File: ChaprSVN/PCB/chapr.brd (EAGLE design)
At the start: 70.9 x 54.1 mm, 20 parts, among them M2 RN42 Module

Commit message: Intermediate version with new power-on circuit.  NOT COMPLETE.
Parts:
- added D1, D2: 1N4148, diode:DO35-7
- added PB2: BUTTON, ChapR-Custom:2-PIN-PUSHBUTTON
- added R12, R13, R15: 12k, resistor:0207/10
- added R14: 22k, resistor:0207/10
- added T1, T2: (no value), transistor:TO92
- moved JP1 18.7 mm to (66.4, 54.0), turned to 0 degrees
- moved R5 16.1 mm to (10.3, 42.1)
- moved R4 16.1 mm to (10.2, 45.7)
- moved R7 15.2 mm to (38.1, 42.2)
- moved R8 15.2 mm to (38.2, 45.6)
- moved R1 15.0 mm to (24.2, 45.6)
- moved R2 14.9 mm to (24.2, 42.0)
- moved R11 6.91 mm to (24.7, 23.4)
- moved R9 6.71 mm to (10.5, 23.5)
- moved R6 6.02 mm to (24.7, 26.5)
- moved R3 5.83 mm to (10.4, 26.5)
- moved ARDUINO 4.00 mm to (17.8, 25.8)
- moved VDIP 2.00 mm to (36.2, 44.2)
- moved U$2 1.00 mm to (61.0, 7.23)
- renumbered LED2 to PWR-LED
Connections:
- net 3.3V renamed +3V3
- new net +5V: ARDUINO.VCC, PB1.P$1, R12.1, VDIP.2, VDIP.3, VDIP.9
- new net N$23: ARDUINO.RAWV, T1.3
- new net N$25: D2.A, R15.2, T2.3
- new net N$26: R13.1, T2.2
- new net N$27: D1.C, D2.C, PB2.P$2
- new net N$29: ARDUINO.A5, D1.A, R12.2
- new net N$30: ARDUINO.A4, R13.2
- net +9V: now also R14.2, T1.1; no longer ARDUINO.RAWV
- net GND: now also PB2.P$1, T2.1
- net N$1: now also R14.1, R15.1, T1.2; no longer ARDUINO.VCC, PB1.P$1, VDIP.2, VDIP.3, VDIP.9
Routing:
- net +5V: track 0.00 -> 168.9 mm, vias 0 -> 4
- net N$25: track 0.00 -> 90.4 mm, vias 0 -> 3
- net N$23: track 0.00 -> 89.3 mm, vias 0 -> 1
- net N$29: track 0.00 -> 79.2 mm, vias 0 -> 1
- net N$1: track 95.2 -> 24.4 mm, vias 1 -> 0
- net +9V: track 84.6 -> 15.2 mm
- net N$22: track 76.9 -> 132.4 mm, vias 0 -> 3
- net GND: track 176.5 -> 222.9 mm
- net N$30: track 0.00 -> 40.7 mm, vias 0 -> 1
- net N$27: track 0.00 -> 33.2 mm
- net N$12: track 65.0 -> 93.6 mm, vias 0 -> 2
- net N$13: track 63.4 -> 36.5 mm, vias 1 -> 2
- net N$18: track 50.5 -> 26.9 mm, vias 1 -> 0
- net N$7: track 40.0 -> 63.5 mm
- net N$14: track 61.8 -> 81.9 mm, vias 0 -> 7
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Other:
- board size 70.9 x 54.1 mm -> 70.9 x 56.2 mm

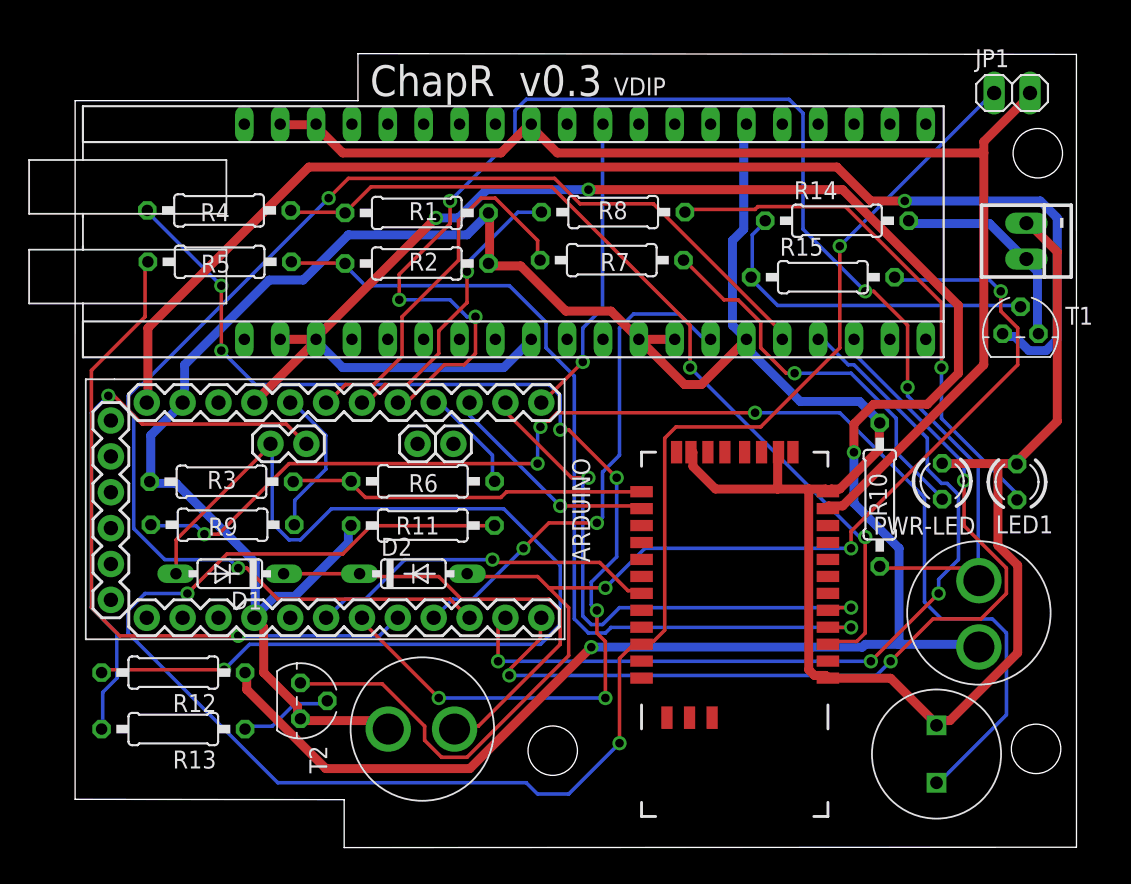
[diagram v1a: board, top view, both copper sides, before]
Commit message: 
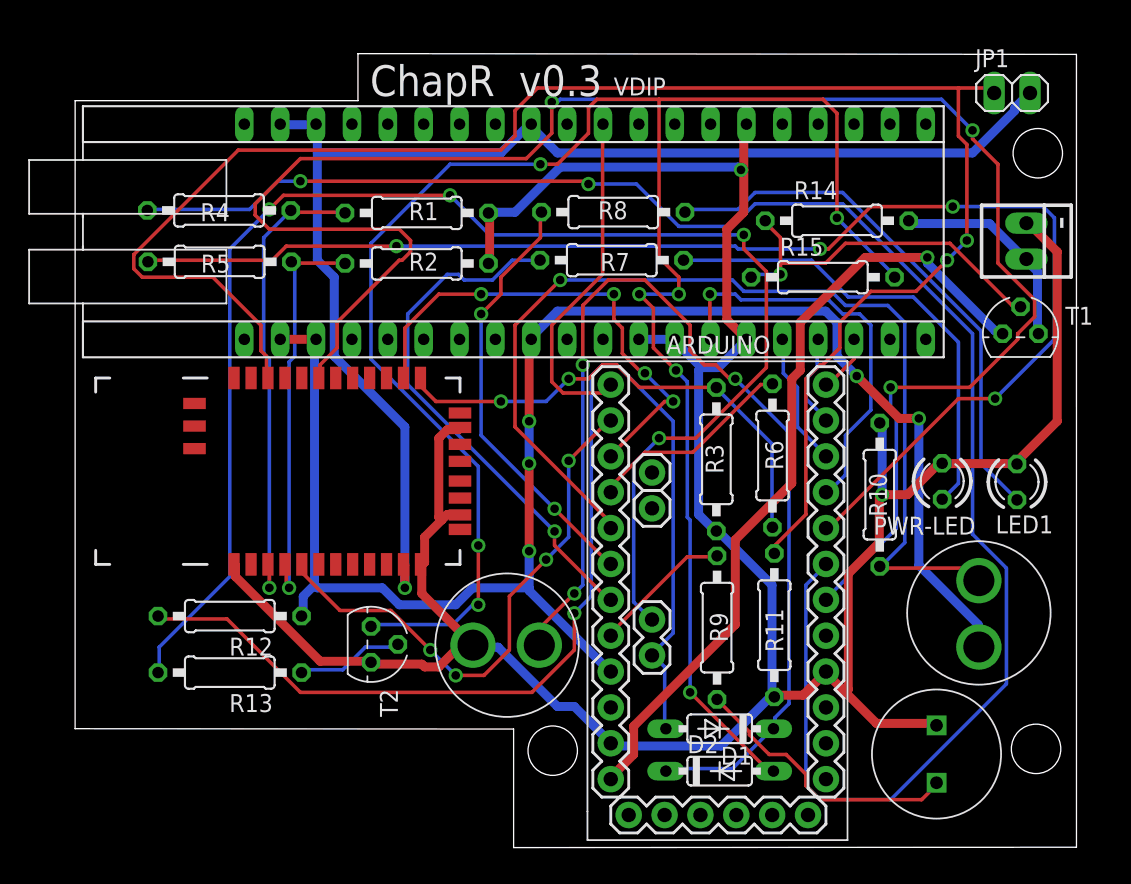
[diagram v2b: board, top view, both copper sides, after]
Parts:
- moved D1 36.4 mm to (45.7, 9.02)
- moved R9 35.8 mm to (45.5, 16.2), turned to 90 degrees
- moved R3 35.1 mm to (45.5, 28.1), turned to 90 degrees
- moved M2 30.0 mm to (17.9, 27.3), turned to 0 degrees
- moved ARDUINO 27.6 mm to (44.3, 18.2), turned to 180 degrees
- moved R11 25.9 mm to (49.6, 16.4), turned to 90 degrees
- moved D2 25.8 mm to (45.7, 6.02)
- moved R6 24.8 mm to (49.4, 28.4), turned to 90 degrees
- moved PB2 8.44 mm to (30.0, 14.9)
- moved T2 6.40 mm to (21.0, 15.0)
- moved R12 5.66 mm to (11.0, 17.0)
- moved R13 5.66 mm to (11.0, 13.0)
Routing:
- net N$15: track 25.0 -> 126.0 mm, vias 1 -> 3
- net N$12: track 93.6 -> 9.54 mm, vias 2 -> 0
- net N$19: track 89.4 -> 19.6 mm, vias 4 -> 0
- net N$30: track 40.7 -> 105.1 mm, vias 1 -> 4
- net N$10: track 65.1 -> 4.12 mm, vias 3 -> 0
- net N$25: track 90.4 -> 144.0 mm, vias 3 -> 8
- net +5V: track 168.9 -> 115.6 mm, vias 4 -> 5
- net N$11: track 59.9 -> 6.67 mm, vias 3 -> 0
- net N$8: track 49.2 -> 96.6 mm, vias 1 -> 4
- net N$27: track 33.2 -> 76.5 mm, vias 0 -> 3
- net N$14: track 81.9 -> 125.2 mm, vias 7 -> 2
- net N$7: track 63.5 -> 29.0 mm
- net N$23: track 89.3 -> 56.6 mm
- net N$6: track 63.4 -> 33.3 mm, vias 2 -> 1
- net N$24: track 99.4 -> 72.8 mm, vias 5 -> 1
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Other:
- outline, holes or cut-outs redrawn

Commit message: 
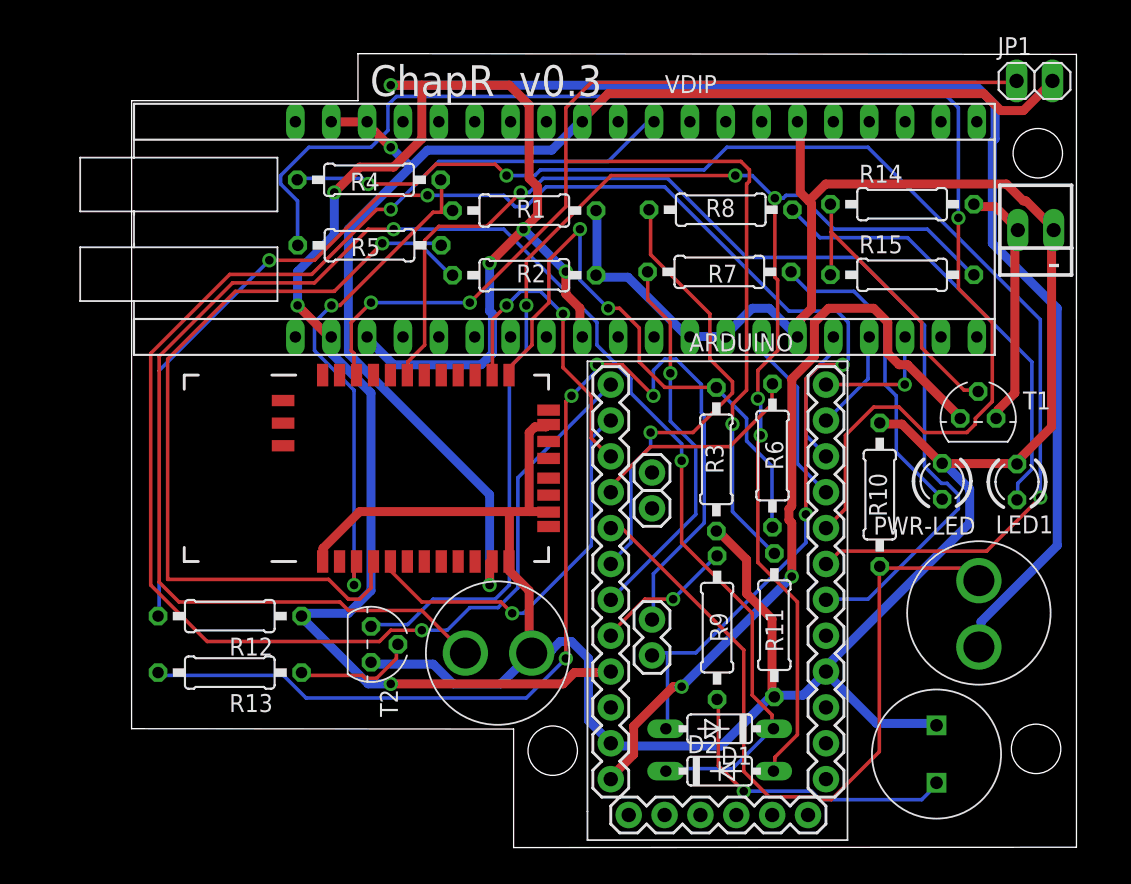
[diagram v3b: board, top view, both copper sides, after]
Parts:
- moved R4 10.8 mm to (20.9, 47.9)
- moved R5 10.7 mm to (20.9, 43.3)
- moved R2 7.66 mm to (31.9, 41.1)
- moved R7 7.66 mm to (45.7, 41.4)
- moved R1 7.62 mm to (31.9, 45.7)
- moved R8 7.62 mm to (45.8, 45.8)
- moved T1 6.71 mm to (64.0, 31.0)
- moved M2 6.28 mm to (24.2, 27.5)
- moved R15 5.62 mm to (58.6, 41.2)
- moved R14 4.76 mm to (58.6, 46.2)
- moved VDIP 3.62 mm to (39.8, 44.4)
- moved JP1 1.81 mm to (68.0, 54.9)
- moved - 1.02 mm to (68.1, 44.3), turned to 180 degrees
- moved PB2 0.82 mm to (30.6, 14.4), turned to 180 degrees
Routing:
- net +5V: track 115.6 -> 208.3 mm, vias 5 -> 7
- net N$2: track 24.5 -> 105.2 mm, vias 0 -> 2
- net N$15: track 126.0 -> 77.8 mm, vias 3 -> 1
- net N$27: track 76.5 -> 120.0 mm, vias 3 -> 2
- net N$14: track 125.2 -> 89.4 mm, vias 2 -> 3
- net N$29: track 83.5 -> 113.7 mm, vias 1 -> 4
- net N$7: track 29.0 -> 59.0 mm
- net N$25: track 144.0 -> 115.0 mm, vias 8 -> 5
- net N$30: track 105.1 -> 82.0 mm
- net N$22: track 123.5 -> 104.3 mm, vias 2 -> 3
- net N$24: track 72.8 -> 54.0 mm, vias 1 -> 0
- net N$13: track 28.7 -> 12.9 mm, vias 1 -> 0
- net N$4: track 34.9 -> 22.0 mm, vias 4 -> 2
- net N$16: track 33.5 -> 22.4 mm
- net N$5: track 38.3 -> 27.6 mm, vias 4 -> 1
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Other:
- board size 70.9 x 56.2 mm -> 66.9 x 56.2 mm

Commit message: 
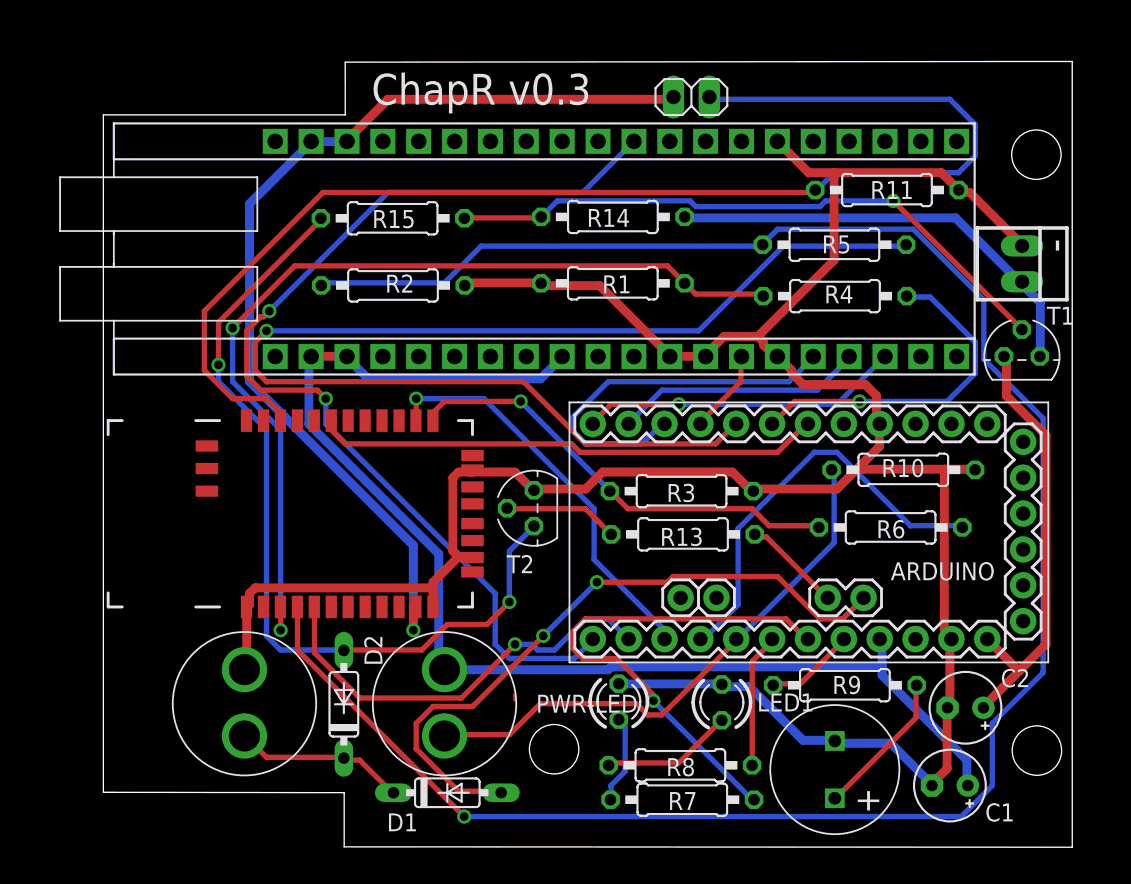
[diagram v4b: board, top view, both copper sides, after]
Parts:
- removed R12: 12k, resistor:0207/10
- removed VDIP: VDIP2, ChapR-Custom:VDIP2
- added C1, C2: (no value), resistor:E2,5-5
- added U$3: VDIP2BIGHOLE, ChapR-Custom:VDIP2-BIGHOLE
- R13, R15: value 12k -> 10k
- R14: value 22k -> 19.1k
- T1: value (none) -> 3906
- T2: value (none) -> 3904
- moved R8 39.5 mm to (42.9, 6.43), turned to 0 degrees
- moved PB1 38.2 mm to (26.2, 11.4), turned to 270 degrees
- moved R7 37.5 mm to (43.0, 4.00), turned to 0 degrees
- moved R15 36.3 mm to (22.5, 45.2), turned to 180 degrees
- moved R4 34.0 mm to (53.9, 39.7), turned to 0 degrees
- moved R13 33.6 mm to (43.1, 22.8), turned to 0 degrees
- moved R5 32.9 mm to (53.8, 43.3), turned to 0 degrees
- moved R11 31.8 mm to (57.5, 47.2), turned to 180 degrees
- moved PWR-LED 27.7 mm to (38.5, 10.9)
- moved D2 27.0 mm to (19.1, 10.8), turned to 90 degrees
- moved LED1 26.1 mm to (45.8, 10.9)
- moved JP1 24.3 mm to (43.7, 53.8), turned to 180 degrees
- moved R14 20.5 mm to (38.1, 45.3)
- moved D1 19.8 mm to (26.4, 4.49), turned to 0 degrees
- moved PB2 18.8 mm to (12.0, 11.4), turned to 270 degrees
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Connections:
- net +3V3: now also U$3.38, U$3.39; no longer VDIP.32, VDIP.38, VDIP.39
- net +5V: now also C1.+, U$3.2, U$3.3, U$3.9; no longer R12.1, VDIP.2, VDIP.3, VDIP.9
- net GND: now also C1.-, C2.-, U$3.12, U$3.13, U$3.15, U$3.26; no longer VDIP.12, VDIP.13, VDIP.15, VDIP.26
- net LED1(BD5): now also U$3.4; no longer VDIP.4
- net LED2(BD6): now also U$3.5; no longer VDIP.5
- net N$10: now also U$3.18; no longer VDIP.18
- net N$11: now also U$3.17; no longer VDIP.17
- net N$12: now also U$3.16; no longer VDIP.16
- net N$13: now also U$3.14; no longer VDIP.14
- net N$2: now also U$3.30; no longer VDIP.30
- net N$23: now also C2.+
- net N$29: no longer R12.2
- net NC(1): now also U$3.1; no longer VDIP.1
- net NC(2): now also U$3.40; no longer VDIP.40
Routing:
- net +5V: track 208.3 -> 89.4 mm, vias 7 -> 0
- net N$27: track 120.0 -> 12.2 mm, vias 2 -> 0
- net N$7: track 59.0 -> 146.4 mm
- net N$30: track 82.0 -> 7.11 mm, vias 4 -> 0
- net N$29: track 113.7 -> 47.0 mm, vias 4 -> 2
- net N$14: track 89.4 -> 24.3 mm, vias 3 -> 1
- net N$25: track 115.0 -> 59.1 mm, vias 5 -> 2
- net N$15: track 77.8 -> 35.9 mm, vias 1 -> 0
- net N$2: track 105.2 -> 72.7 mm
- net N$6: track 36.9 -> 64.7 mm
- net N$20: track 32.8 -> 9.52 mm, vias 1 -> 0
- net +3V3: track 93.4 -> 70.1 mm, vias 2 -> 1
- net N$23: track 54.1 -> 31.1 mm, vias 2 -> 0
- net N$1: track 21.2 -> 44.1 mm, vias 0 -> 1
- net N$17: track 31.6 -> 9.33 mm
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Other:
- board size 66.9 x 56.2 mm -> 68.6 x 55.6 mm
- board text added: "+"
- board text added: ".26 inner support diam"
- board text added: ".32 outer support diam"
- board text added: "1.94 between outer supports edge"
- board text added: "2.4 max board width"

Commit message: 
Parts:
- T1, T2: device transistor:TO92 -> transistor-neu-to92:TO92-EBC
- moved T2 20.9 mm to (34.4, 3.79), turned to 0 degrees
- moved T1 1.09 mm to (68.0, 36.0), turned to 270 degrees
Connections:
- net +3V3: now also U$3.32
- net +9V: now also T1.E; no longer T1.1
- net GND: now also T2.C; no longer T2.1
- net N$1: now also T1.B; no longer T1.2
- net N$23: now also T1.C; no longer T1.3
- net N$25: now also T2.E; no longer T2.3
- net N$26: now also T2.B; no longer T2.2
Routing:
- net N$7: track 146.4 -> 69.2 mm, vias 1 -> 2
- net N$11: track 17.7 -> 82.0 mm, vias 0 -> 2
- net N$8: track 87.8 -> 30.7 mm
- net N$2: track 72.7 -> 102.6 mm, vias 2 -> 1
- net GND: track 191.8 -> 219.8 mm, vias 0 -> 1
- net N$18: track 36.4 -> 13.5 mm
- net N$26: track 8.13 -> 24.9 mm, vias 0 -> 1
- net N$12: track 27.3 -> 13.0 mm
- net N$1: track 44.1 -> 53.5 mm, vias 1 -> 0
- net N$3: track 29.6 -> 21.8 mm
- net N$5: track 30.1 -> 25.7 mm
- net N$25: track 59.1 -> 63.1 mm
- net N$4: track 28.8 -> 25.2 mm, vias 1 -> 0
- net +5V: track 89.4 -> 85.8 mm
- net +9V: track 31.7 -> 28.1 mm
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
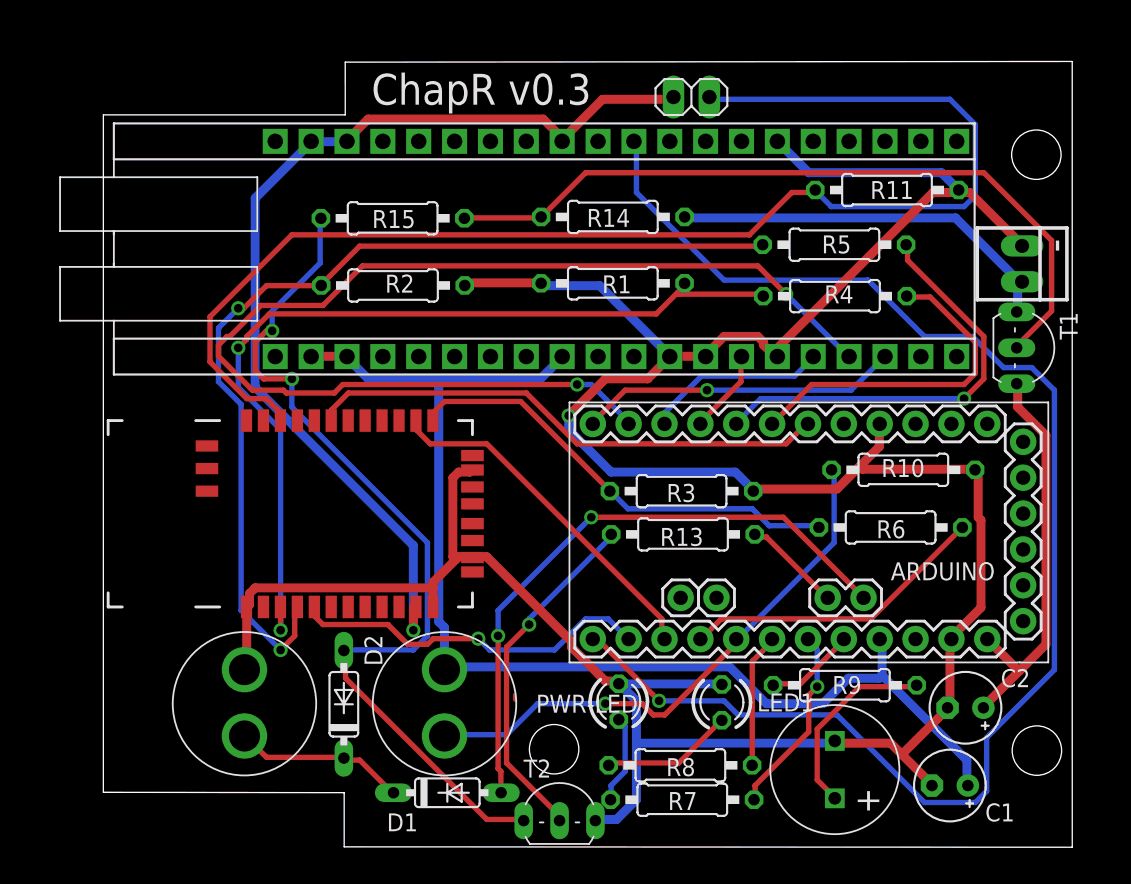
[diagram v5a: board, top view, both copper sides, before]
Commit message: 
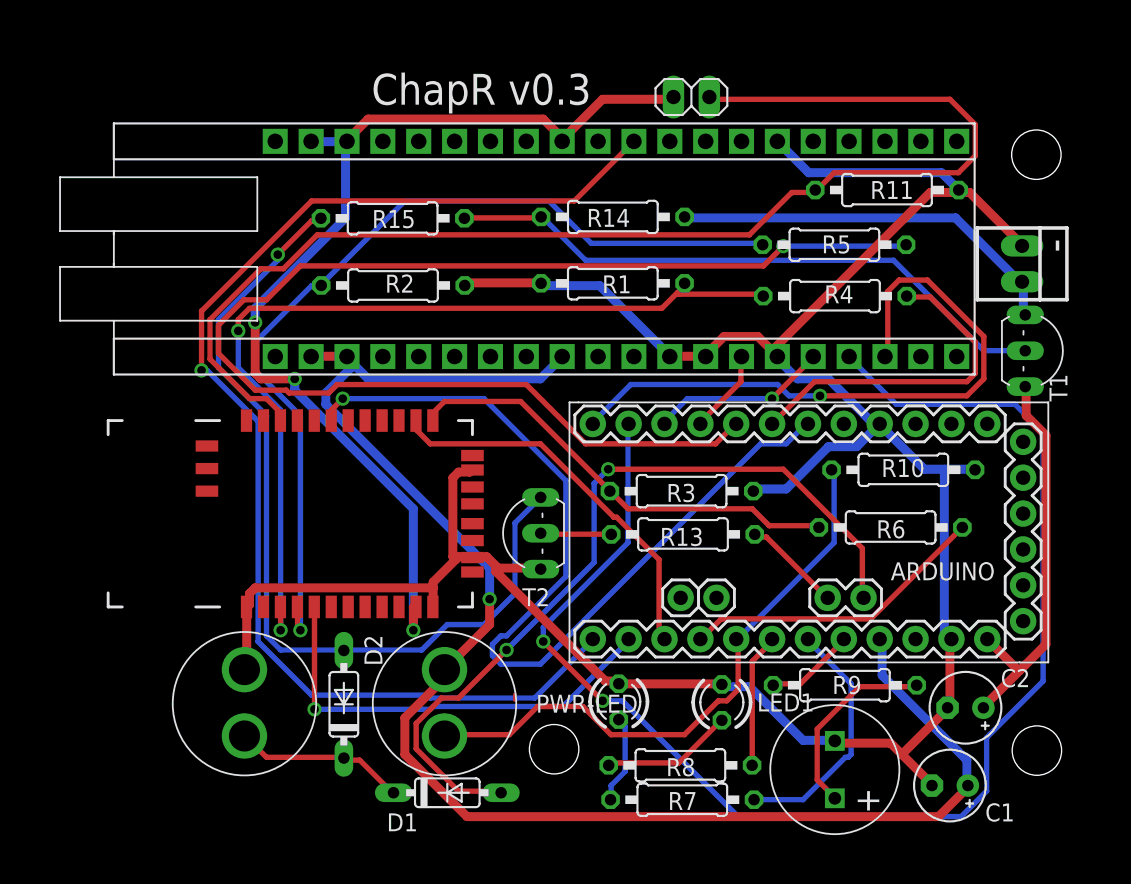
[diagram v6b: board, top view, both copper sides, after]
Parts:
- moved T2 19.3 mm to (31.7, 22.9), turned to 90 degrees
- moved T1 0.64 mm to (68.6, 35.8)
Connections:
- net GND: now also T2.E; no longer T2.C
- net N$25: now also T2.C; no longer T2.E
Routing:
- net N$8: track 30.7 -> 93.5 mm
- net GND: track 219.8 -> 189.0 mm, vias 1 -> 0
- net N$15: track 37.1 -> 64.5 mm, vias 0 -> 1
- net +5V: track 85.8 -> 111.0 mm, vias 0 -> 1
- net N$10: track 22.7 -> 46.3 mm
- net N$26: track 24.9 -> 5.01 mm, vias 1 -> 0
- net N$11: track 82.0 -> 98.3 mm
- net N$2: track 102.6 -> 88.0 mm
- net N$29: track 44.0 -> 57.3 mm
- net N$1: track 53.5 -> 43.7 mm
- net N$5: track 25.7 -> 31.6 mm
- net N$7: track 69.2 -> 64.8 mm, vias 2 -> 1
- net N$18: track 13.5 -> 17.6 mm, vias 1 -> 0
- net N$24: track 39.4 -> 42.4 mm, vias 1 -> 0
- net N$22: track 93.8 -> 90.9 mm
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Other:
- board outline removed
